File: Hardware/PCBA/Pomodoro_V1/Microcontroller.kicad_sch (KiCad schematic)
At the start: 0 parts

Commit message: Updated CubeMx File, Created Schematic for µC, layouted the LEDs on the PCB
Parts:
- added C18, C20: 4u7, symbol Device:C
- added C19, C21: 100n, symbol Device:C
- added J1: Conn_01x10_Pin, symbol Connector:Conn_01x10_Pin
- added U1: STM32G071RBTx, Package_QFP:LQFP-64_10x10mm_P0.5mm, symbol MCU_ST_STM32G0:STM32G071RBTx
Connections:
- new net +3V3: C18.1, C19.1, C20.1, C21.1, J1.1 (Pin_1), U1.6 (VBAT), U1.7 (VREF+), U1.8 (VDD)
- new net +5V: J1.8 (Pin_8), J1.9 (Pin_9)
- new net GND: C18.2, C19.2, C20.2, C21.2, J1.3 (Pin_3), J1.5 (Pin_5), J1.6 (Pin_6), J1.7 (Pin_7), U1.9 (VSS)
- new net GPIO_IN (Encoder BTN): U1.16 (PC3)
- new net GPIO_IN (Trigger Btn): U1.3 (PC13)
- new net GPIO_OUT (Blinky Led): U1.22 (PA5)
- new net GPIO_OUT (Debug 1): U1.55 (PD5)
- new net GPIO_OUT (Debug 2): U1.56 (PD6)
- new net GPIO_OUT (Debug 3): U1.41 (PD9)
- new net GPIO_OUT (Debug 4): U1.39 (PC7)
- new net I2C1_SCL: U1.60 (PB6)
- new net I2C1_SDA: U1.61 (PB7)
- new net NRST: J1.10 (Pin_10), U1.12 (PF2)
- new net SWCLK: J1.4 (Pin_4), U1.46 (PA14)
- new net SWDIO: J1.2 (Pin_2), U1.45 (PA13)
- new net TIM1_CH1 (RgbLed): U1.36 (PA8)
- new net TIM2_CH1 (Encoder): U1.17 (PA0)
- new net TIM2_CH2 (Encoder): U1.18 (PA1)
- new net USART1_RX: U1.26 (PC5)
- new net USART1_TX: U1.25 (PC4)
- new net USART2_RX: U1.20 (PA3)
- new net USART2_TX: U1.19 (PA2)
- no-connect marks 0 -> 40
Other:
- note added: "Debug and Flashing Connector"
- note added: "Microcontroller"
- note added: "µC Powersupply See Datasheet: DS12232 Rev 4 Page 53/135"

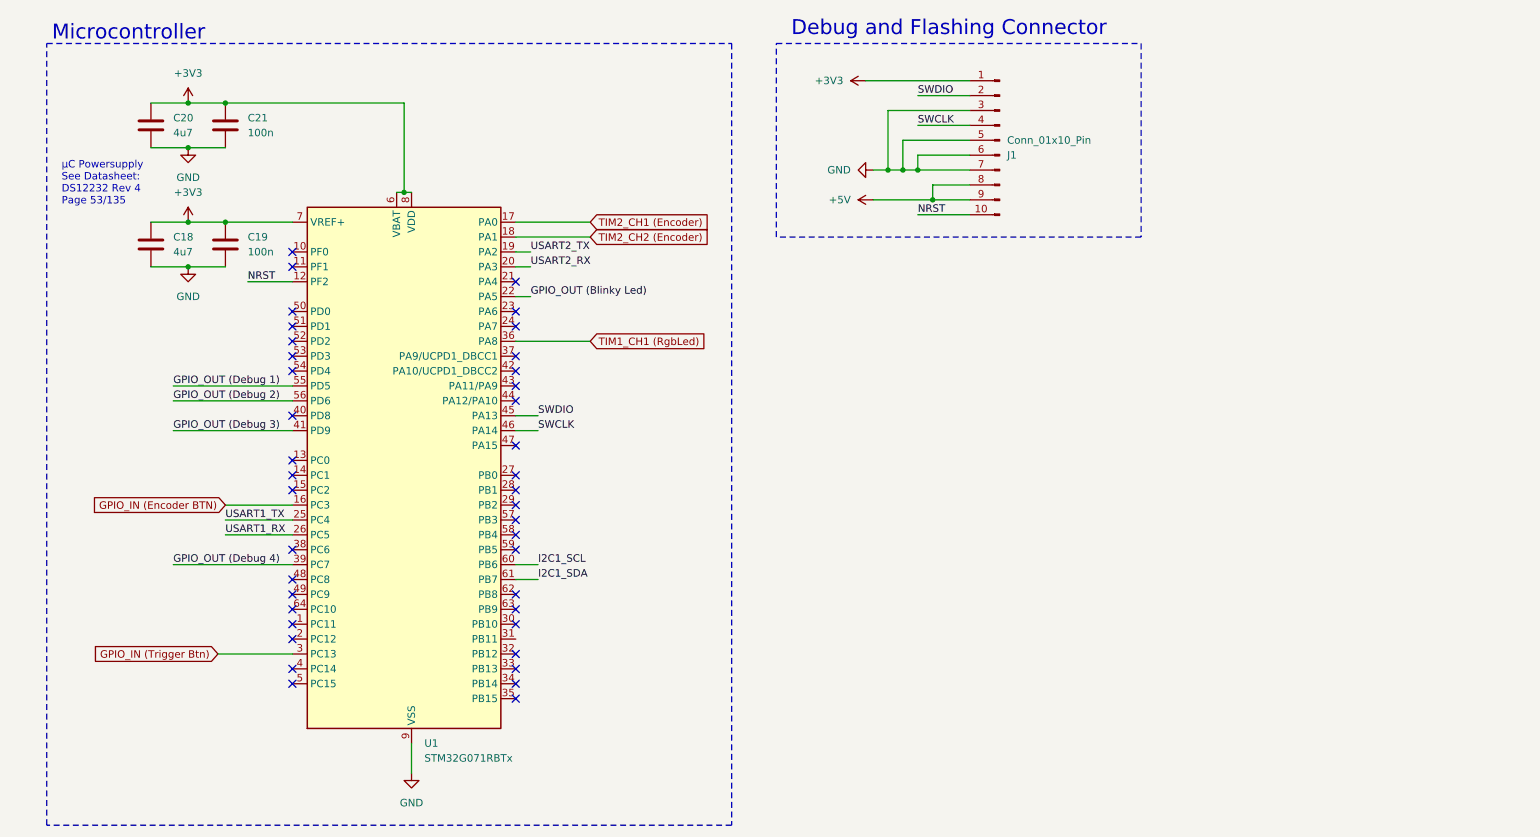
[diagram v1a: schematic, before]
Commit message: added the accelerometer to the Schematic
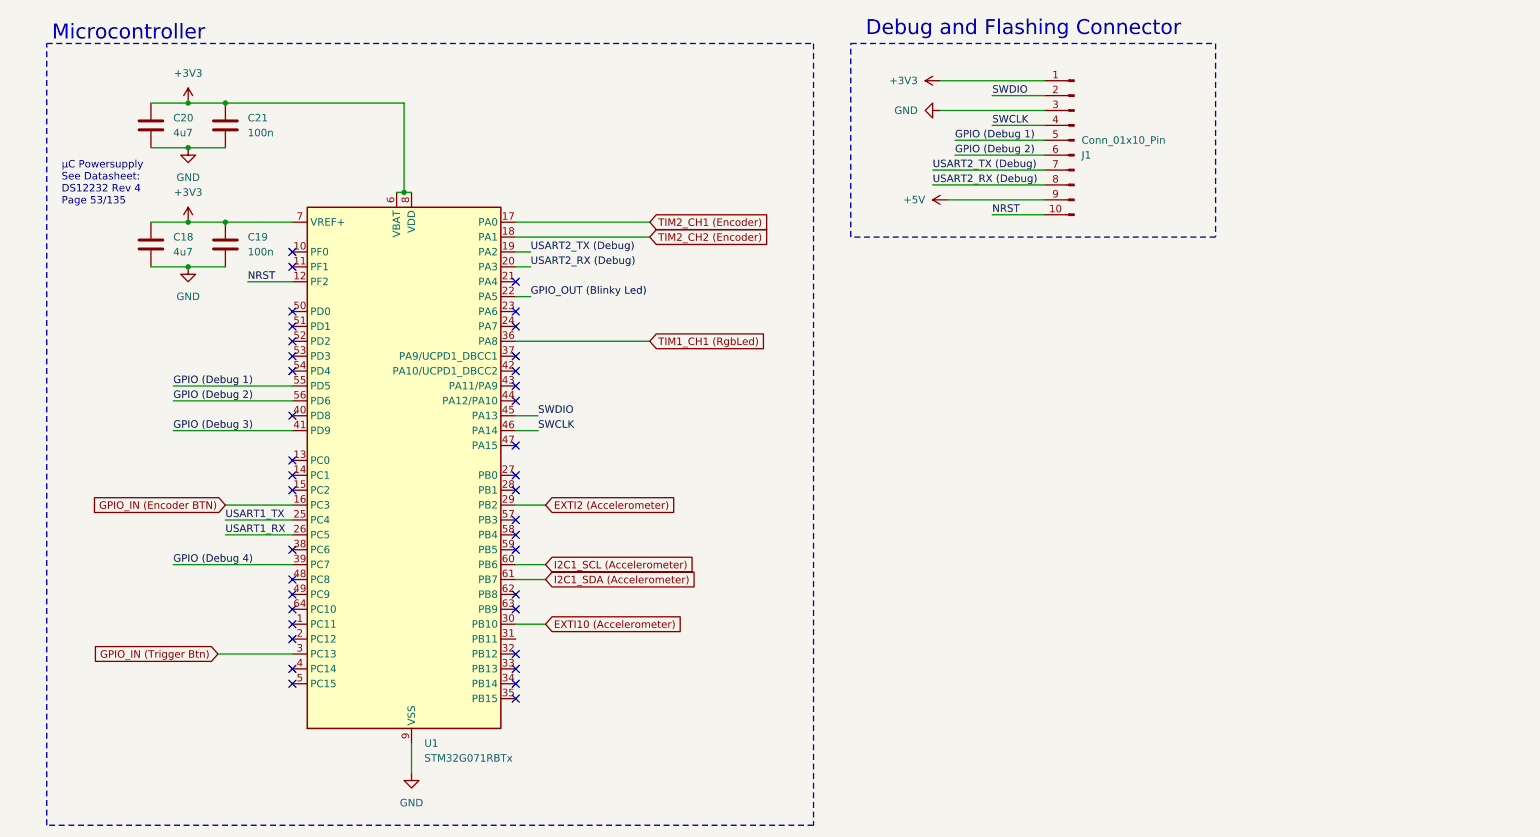
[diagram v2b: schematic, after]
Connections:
- net +5V: no longer J1.8 (Pin_8)
- net GND: no longer J1.5 (Pin_5), J1.6 (Pin_6), J1.7 (Pin_7)
- net EXTI2 (Accelerometer): now reaches U1.29 (PB2)
- net EXTI10 (Accelerometer): now reaches U1.30 (PB10)
- net GPIO_OUT (Debug 1) renamed GPIO (Debug 1)
- net GPIO (Debug 1): now also J1.5 (Pin_5)
- net GPIO_OUT (Debug 2) renamed GPIO (Debug 2)
- net GPIO (Debug 2): now also J1.6 (Pin_6)
- net GPIO_OUT (Debug 3) renamed GPIO (Debug 3)
- net GPIO_OUT (Debug 4) renamed GPIO (Debug 4)
- net I2C1_SCL renamed I2C1_SCL (Accelerometer)
- net I2C1_SDA renamed I2C1_SDA (Accelerometer)
- net USART2_RX renamed USART2_RX (Debug)
- net USART2_RX (Debug): now also J1.8 (Pin_8)
- net USART2_TX renamed USART2_TX (Debug)
- net USART2_TX (Debug): now also J1.7 (Pin_7)
- no-connect marks 40 -> 38
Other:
- moved on the sheet: J1

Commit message: Implemented the Rotary encoder, the buttons, the IMU, Added it to the PCB (All the space constraining elements are now placed)
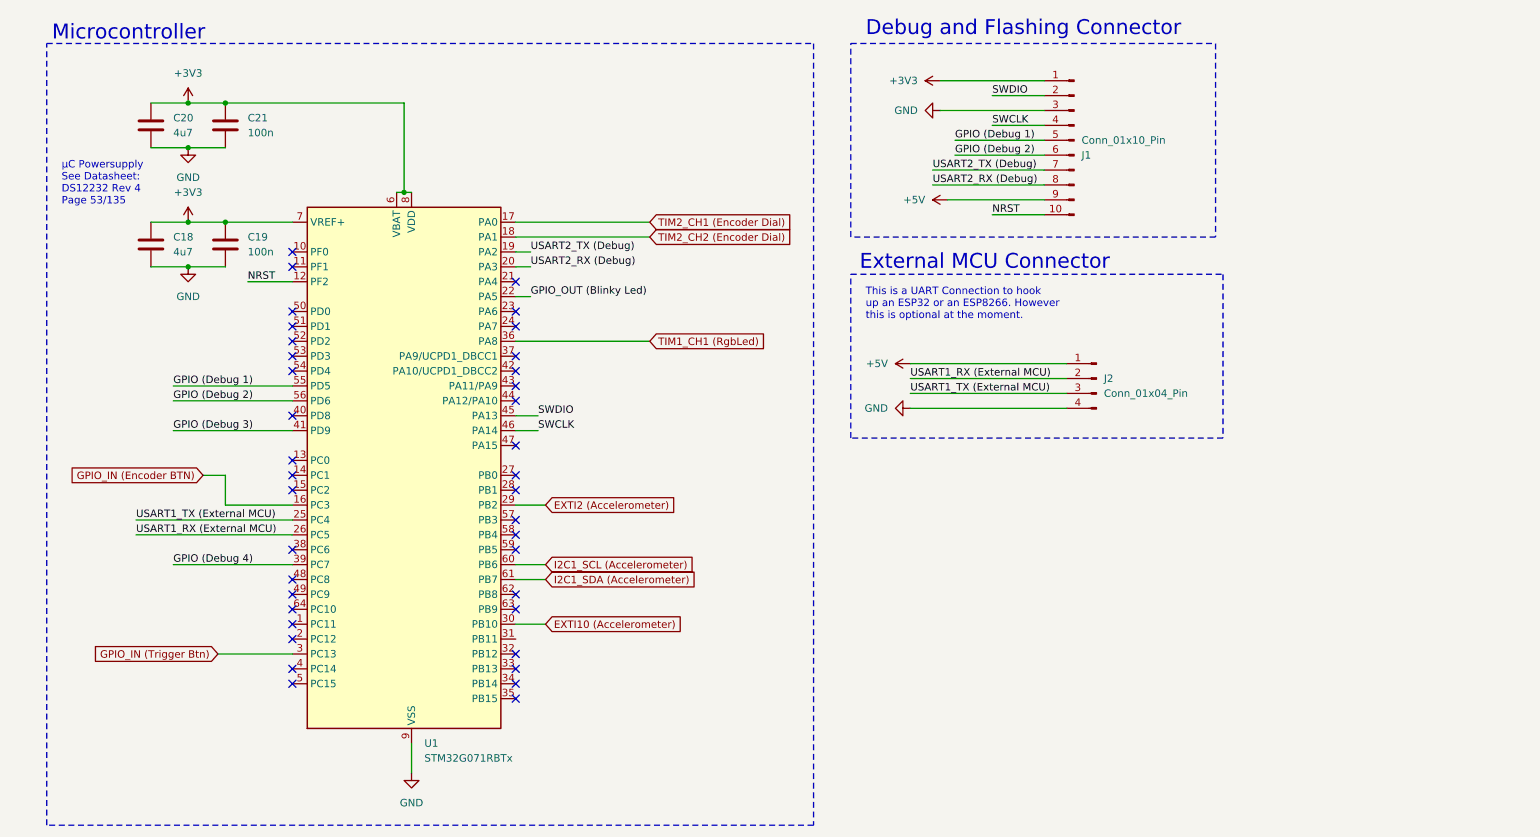
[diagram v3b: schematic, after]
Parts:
- added J2: Conn_01x04_Pin, symbol Connector:Conn_01x04_Pin
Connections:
- net +5V: now also J2.1 (Pin_1)
- net GND: now also J2.4 (Pin_4)
- net TIM2_CH1 (Encoder) renamed TIM2_CH1 (Encoder Dial)
- net TIM2_CH2 (Encoder) renamed TIM2_CH2 (Encoder Dial)
- net USART1_RX renamed USART1_RX (External MCU)
- net USART1_RX (External MCU): now also J2.2 (Pin_2)
- net USART1_TX renamed USART1_TX (External MCU)
- net USART1_TX (External MCU): now also J2.3 (Pin_3)
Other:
- note added: "External MCU Connector"
- note added: "This is a UART Connection to hook up an ESP32 or an ESP8266. However this is optional at the moment."

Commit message: Finalized the schematic, First Draft of the finished Layout
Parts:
- removed C20: 4u7, symbol Device:C
- added C31: 100n, Capacitor_SMD:C_0805_2012Metric, symbol Device:C
- added D109: LED, Resistor_SMD:R_0603_1608Metric, symbol Device:LED
- added J1, J4, J5, J6, J7: Conn_01x02_Pin, Connector_PinHeader_2.54mm:PinHeader_1x02_P2.54mm_Vertical, symbol Connector:Conn_01x02_Pin
- added J3: Conn_01x03_Pin, Connector_PinHeader_2.54mm:PinHeader_1x03_P2.54mm_Vertical, symbol Connector:Conn_01x03_Pin
- added R13: 270, Resistor_SMD:R_0805_2012Metric, symbol Device:R
- C18, C19, C21: footprint (none) -> Capacitor_SMD:C_0805_2012Metric
- J2: renamed from J1; footprint (none) -> Connector:Tag-Connect_TC2050-IDC-NL_2x05_P1.27mm_Vertical
- J9: renamed from J2; footprint (none) -> Connector_PinHeader_2.54mm:PinHeader_1x04_P2.54mm_Vertical; now not fitted
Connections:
- net +3V3: now also C18.2, C19.2, C21.2, J1.1 (Pin_1), R13.1; no longer C18.1, C19.1, C21.1
- net +5V: now also J4.2 (Pin_2)
- net GND: now also C18.1, C19.1, C21.1, C31.1, J1.2 (Pin_2), J4.1 (Pin_1); no longer C18.2, C19.2, C21.2
- net GPIO (Debug 1): now also J5.1 (Pin_1)
- net GPIO (Debug 2): now also J5.2 (Pin_2)
- net GPIO (Debug 3): now also J6.1 (Pin_1)
- net GPIO (Debug 4): now also J6.2 (Pin_2)
- net GPIO_OUT (Blinky Led): now also D109.1 (K)
- net NRST: now also C31.2, J3.1 (Pin_1)
- net SWCLK: now also J3.3 (Pin_3)
- net SWDIO: now also J3.2 (Pin_2)
- net USART2_RX (Debug): now also J7.2 (Pin_2)
- net USART2_TX (Debug): now also J7.1 (Pin_1)
- net EXTI8 (Accelerometer): now reaches U1.62 (PB8)
- net EXTI9 (Accelerometer): now reaches U1.63 (PB9)
- net EXTI10 (Accelerometer): no longer names the net of U1.30 (PB10)
- net EXTI2 (Accelerometer): no longer names the net of U1.29 (PB2)
- net TIM1_CH1 (RgbLed) renamed TIM1_CH1 (RgbLed Outer Ring)
- new net: D109.2 (A), R13.2
- no-connect marks 38 -> 39
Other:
- note added: "12mA Current"
- note added: "Blinky LED"
- moved on the sheet: J2

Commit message: Version that was ordered online
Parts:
- C18: value 4u7 -> 1u; Digikey (none) -> https://www.digikey.pt/en/products/detail/nextgen-component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; MPN (none) -> 0805B105K250DC
- C19, C21, C31: Digikey (none) -> https://www.digikey.pt/en/products/detail/yageo/CC0805KRX7R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; MPN (none) -> CC0805KRX7R9BB104
- D109: MPN (none) -> 150060GS55040
- J1, J2, J3, J4, J5, J6, J7, J9: now left out of the parts list
- R13: Digikey (none) -> https://www.digikey.pt/en/products/detail/yageo/RC0805JR-07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; MPN (none) -> RC0805JR-07270RL
- U1: MPN (none) -> STM32G071RBT6

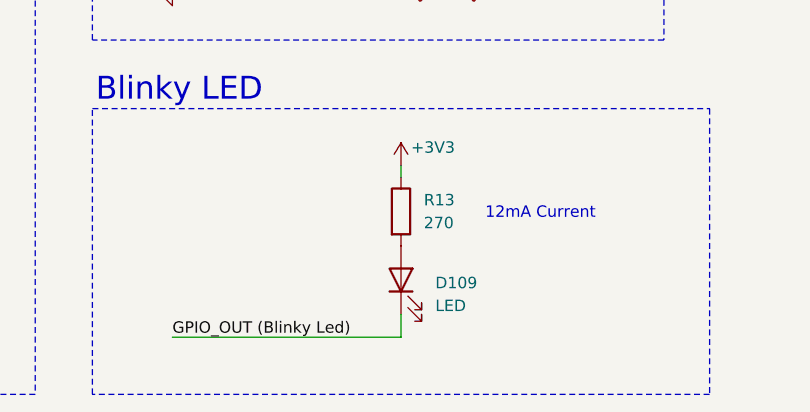
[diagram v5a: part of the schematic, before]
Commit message: Minor refactoring on the RGBLED Driver, Changed the nominalPomodoro Script a bit, Added some dimensions into Kicad
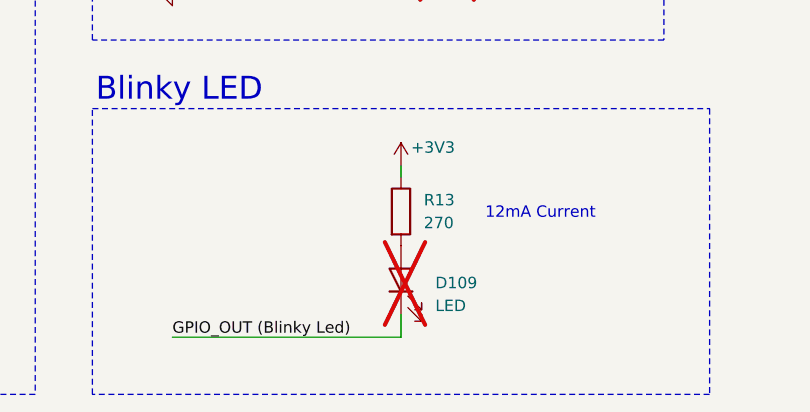
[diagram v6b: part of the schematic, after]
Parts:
- D109: now not fitted
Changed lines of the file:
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@@
 		(in_bom yes)
 		(on_board yes)
-		(dnp no)
+		(dnp yes)
 		(fields_autoplaced yes)
 		(property "Reference" "D109"
